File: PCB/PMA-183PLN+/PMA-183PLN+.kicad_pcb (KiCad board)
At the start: 4 copper layers, 35 x 35 mm, 25 parts, among them U1 PMA-183PLN+, U2 MIC5219-2.6YM5-TR

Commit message: pcb: added boms, updated readmes, changed silkscreen from dfs/ems to nmsm
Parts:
- renumbered RF-In to J1, RF-Out to J2, GND to TP1, Vin to TP2, 2.6VDC to TP3
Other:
- board text added: "NMSM"
- board text removed: "RF-EMS"
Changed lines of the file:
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@@
     (property "ki_keywords" "test point tp")
     (attr through_hole)
-    (fp_text reference "GND" (at -2 0) (layer "F.SilkS")
+    (fp_text reference "TP1" (at -2 0) (layer "F.Fab")
         (effects (font (size 1 1) (thickness 0.15)) (justify right))
     )
@@
         (effects (font (size 1 1) (thickness 0.15)))
     )
-    (fp_text user "${REFERENCE}" (at 0.7 2.5) (layer "F.Fab") hide
-        (effects (font (size 1 1) (thickness 0.15)))
+    (fp_text user "GND" (at -2 0) (layer "F.SilkS")
+        (effects (font (size 1 1) (thickness 0.15)) (justify right))
     )
     (fp_circle (center 0 0) (end 1.7 0)
@@
     (property "ki_keywords" "BNC SMA SMB SMC LEMO coaxial connector CINCH RCA")
     (attr smd)
-    (fp_text reference "RF-Out" (at -3.84 5.55) (layer "F.SilkS")
+    (fp_text reference "J2" (at -3.84 5.55) (layer "F.Fab")
         (effects (font (size 1 1) (thickness 0.15)) (justify right))
     )
@@
         (effects (font (size 1 1) (thickness 0.15)))
     )
-    (fp_text user "${REFERENCE}" (at -1.5 7) (layer "F.Fab")
-        (effects (font (size 1 1) (thickness 0.15)))
+    (fp_text user "RF-Out" (at -3.84 5.55) (layer "F.SilkS")
+        (effects (font (size 1 1) (thickness 0.15)) (justify right))
     )
     (fp_circle (center -2.9718 -1.2192) (end -2.5654 -1.2192)
@@
     (property "ki_keywords" "test point tp")
     (attr through_hole)
-    (fp_text reference "2.6VDC" (at -2 0) (layer "F.SilkS")
+    (fp_text reference "TP3" (at -2 0) (layer "F.Fab")
         (effects (font (size 1 1) (thickness 0.15)) (justify right))
     )
@@
         (effects (font (size 1 1) (thickness 0.15)))
     )
-    (fp_text user "${REFERENCE}" (at 0.7 2.5) (layer "F.Fab")
-        (effects (font (size 1 1) (thickness 0.15)))
+    (fp_text user "2.6VDC" (at -2 0) (layer "F.SilkS")
+        (effects (font (size 1 1) (thickness 0.15)) (justify right))
     )
     (fp_circle (center 0 0) (end 1.7 0)
@@
     (property "ki_keywords" "test point tp")
     (attr through_hole)
-    (fp_text reference "Vin" (at -2 0) (layer "F.SilkS")
+    (fp_text reference "TP2" (at -2 0) (layer "F.Fab")
         (effects (font (size 1 1) (thickness 0.15)) (justify right))
     )
@@
         (effects (font (size 1 1) (thickness 0.15)))
     )
-    (fp_text user "${REFERENCE}" (at 0.7 2.5) (layer "F.Fab")
-        (effects (font (size 1 1) (thickness 0.15)))
+    (fp_text user "Vin" (at -2 0) (layer "F.SilkS")
+        (effects (font (size 1 1) (thickness 0.15)) (justify right))
     )
     (fp_circle (center 0 0) (end 1.7 0)
@@
     (property "ki_keywords" "BNC SMA SMB SMC LEMO coaxial connector CINCH RCA")
     (attr smd)
-    (fp_text reference "RF-In" (at -3.84 -5.6) (layer "F.SilkS")
+    (fp_text reference "J1" (at -3.84 -5.6) (layer "F.Fab")
         (effects (font (size 1 1) (thickness 0.15)) (justify left))
     )
@@
         (effects (font (size 1 1) (thickness 0.15)))
     )
-    (fp_text user "${REFERENCE}" (at -1.5 7) (layer "F.Fab")
-        (effects (font (size 1 1) (thickness 0.15)))
+    (fp_text user "RF-In" (at -3.84 -5.6) (layer "F.SilkS")
+        (effects (font (size 1 1) (thickness 0.15)) (justify left))
     )
     (fp_circle (center -2.9718 -1.2192) (end -2.5654 -1.2192)
@@
     (effects (font (size 1 1) (thickness 0.2) bold) (justify right bottom mirror))
   )
-  (gr_text "RF-EMS" (at 147.1 102.5) (layer "F.SilkS")
+  (gr_text "NMSM" (at 147.1 102.5) (layer "F.SilkS")
     (effects (font (size 1.5 1.5) (thickness 0.3) bold) (justify right bottom))
   )

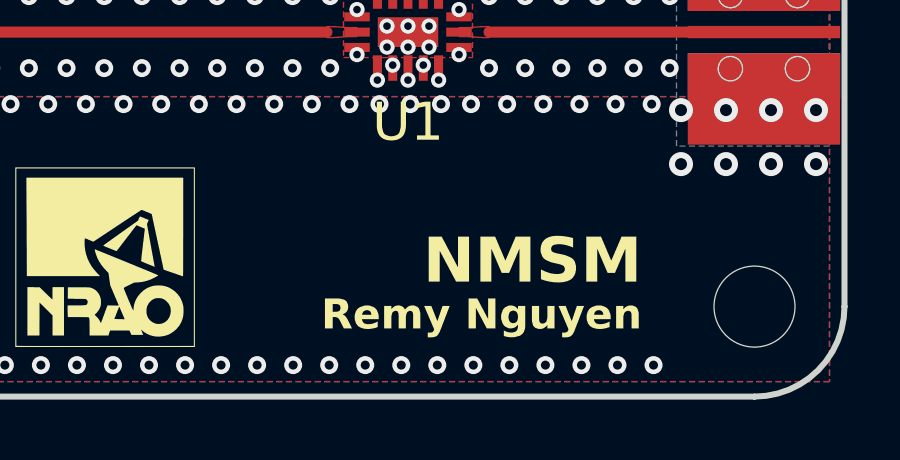
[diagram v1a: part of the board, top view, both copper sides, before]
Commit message: pcb: fixed silkscreen to be consistent with pma3-14ln+ (name, revision, device)
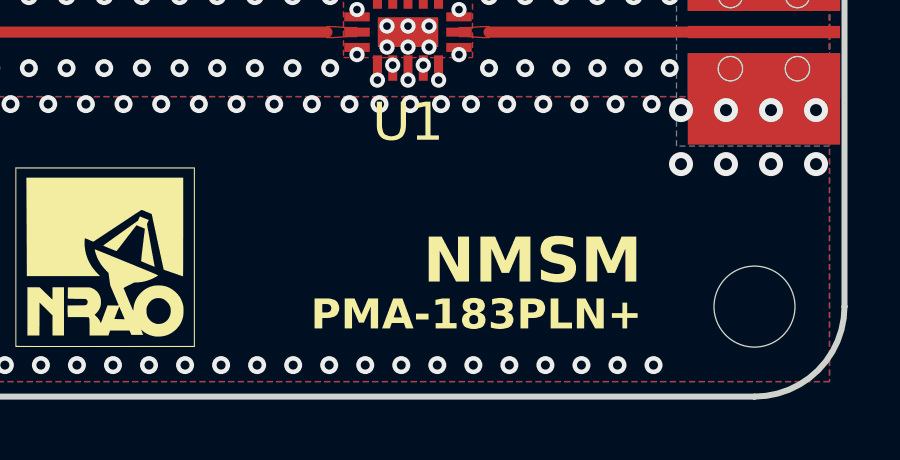
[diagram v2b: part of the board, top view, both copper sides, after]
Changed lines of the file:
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@@
   (gr_line (start 128.45 88.56) (end 128.45 88.74)
     (stroke (width 0.2) (type solid)) (layer "User.9"))
-  (gr_text "PMA-183PLN+" (at 147.1 104) (layer "B.SilkS")
+  (gr_text "Remy Nguyen" (at 147.1 104) (layer "B.SilkS")
     (effects (font (size 1 1) (thickness 0.2) bold) (justify left bottom mirror))
   )
@@
     (effects (font (size 1.5 1.5) (thickness 0.3) bold) (justify right bottom))
   )
-  (gr_text "Remy Nguyen" (at 147.1 104) (layer "F.SilkS")
+  (gr_text "PMA-183PLN+" (at 147.1 104) (layer "F.SilkS")
     (effects (font (size 1 1) (thickness 0.2) bold) (justify right bottom))
   )
